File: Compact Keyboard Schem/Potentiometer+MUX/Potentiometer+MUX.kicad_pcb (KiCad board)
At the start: 2 copper layers, 83.5 x 157 mm, 17 parts, among them J1 Conn_01x04, J2 Conn_01x02, J3 Conn_01x08, J4 Conn_01x16

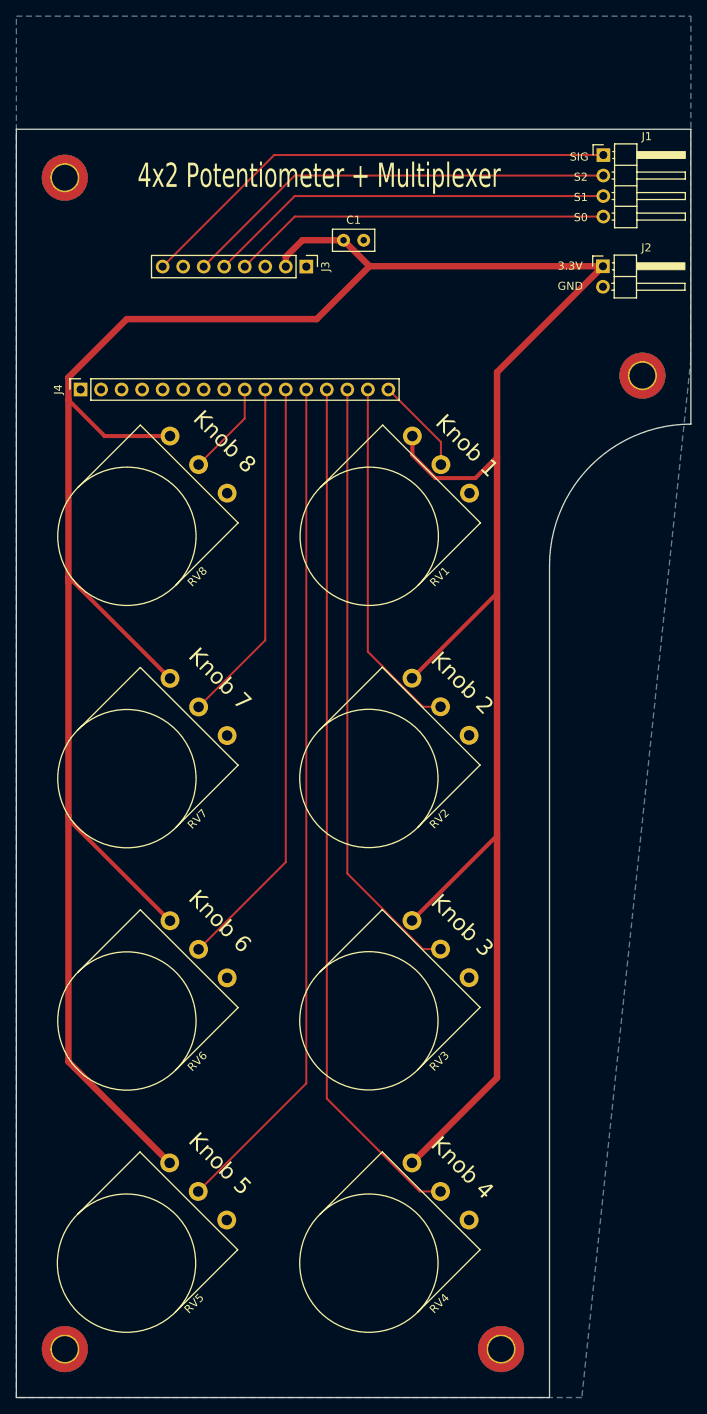
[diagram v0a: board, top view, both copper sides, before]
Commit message: Post PCB Manufacturing
Specifically the Potentiometer+ MUX
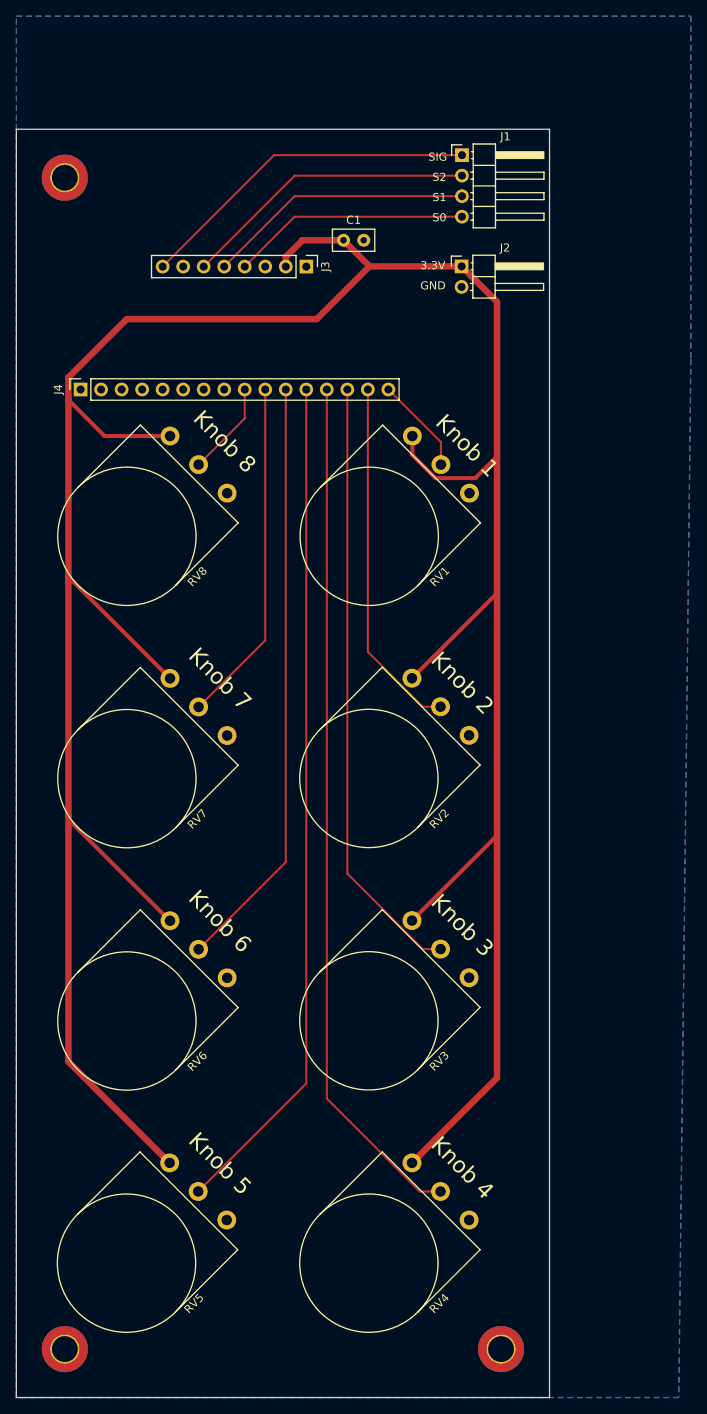
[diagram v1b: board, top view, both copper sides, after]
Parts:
- removed the REF** at (154.5, 60.5)
- moved J1 17.5 mm to (132.2, 33.2)
- moved J2 17.5 mm to (132.1, 47.0)
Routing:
- net +3.3V: track 404.8 -> 383.7 mm
- net Net-(J1-Pin_2): track 54.1 -> 36.6 mm
- net Net-(J1-Pin_4): track 47.0 -> 29.4 mm
- net Net-(J1-Pin_3): track 50.5 -> 33.0 mm
- net Net-(J1-Pin_1): track 60.3 -> 42.8 mm
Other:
- board size 83.5 x 157 mm -> 66 x 157 mm
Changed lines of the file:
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@@
 			(plot_on_all_layers_selection 0x00000000_00000000_00000000_00000000)
 			(disableapertmacros no)
-			(usegerberextensions no)
+			(usegerberextensions yes)
 			(usegerberattributes yes)
 			(usegerberadvancedattributes yes)
@@
 			(crossoutdnponfab yes)
 			(subtractmaskfromsilk no)
-			(outputformat 4)
+			(outputformat 1)
 			(mirror no)
 			(drillshape 0)
 			(scaleselection 1)
-			(outputdirectory "./")
+			(outputdirectory "Manufacturing Files/")
 		)
 	)
@@
 	(footprint "Connector_PinHeader_2.54mm:PinHeader_1x04_P2.54mm_Horizontal"
 		(layer "F.Cu")
-		(at 149.661498 33.19)
+		(at 132.161498 33.205)
 		(descr "Through hole angled pin header, 1x04, 2.54mm pitch, 6mm pin length, single row")
 		(tags "Through hole angled pin header THT 1x04 2.54mm single row")
@@
 	(footprint "MountingHole:MountingHole_3.2mm_M3_ISO7380_Pad_TopBottom"
 		(layer "F.Cu")
-		(at 154.5 60.5)
-		(descr "Mounting Hole 3.2mm, M3, generated by kicad-footprint-generator mountinghole.py")
-		(tags "mountinghole M3 ISO7380")
-		(property "Reference" "REF**"
-			(at 0 -3.8 0)
-			(layer "F.SilkS")
-			(hide yes)
-			(effects
-				(font
-					(size 1 1)
-					(thickness 0.15)
-				)
-			)
-		)
-		(property "Value" "MountingHole_3.2mm_M3_ISO7380_Pad_TopBottom"
-			(at 0 3.8 0)
-			(layer "F.Fab")
-			(effects
-				(font
-					(size 1 1)
-					(thickness 0.15)
-				)
-			)
-		)
-		(property "Datasheet" ""
-			(at 0 0 0)
-			(layer "F.Fab")
-			(hide yes)
-			(effects
-				(font
-					(size 1.27 1.27)
-					(thickness 0.15)
-				)
-			)
-		)
-		(property "Description" ""
-			(at 0 0 0)
-			(layer "F.Fab")
-			(hide yes)
-			(effects
-				(font
-					(size 1.27 1.27)
-					(thickness 0.15)
-				)
-			)
-		)
-		(attr exclude_from_pos_files exclude_from_bom)
-		(fp_circle
-			(center 0 0)
-			(end 2.85 0)
-			(stroke
-				(width 0.15)
-				(type solid)
-			)
-			(fill no)
-			(layer "Cmts.User")
-		)
-		(fp_circle
-			(center 0 0)
-			(end 3.1 0)
-			(stroke
-				(width 0.05)
-				(type solid)
-			)
-			(fill no)
-			(layer "F.CrtYd")
-		)
-		(fp_text user "${REFERENCE}"
-			(at 0 0 0)
-			(layer "F.Fab")
-			(effects
-				(font
-					(size 1 1)
-					(thickness 0.15)
-				)
-			)
-		)
-		(pad "1" thru_hole circle
-			(at 0 0)
-			(size 3.6 3.6)
-			(drill 3.2)
-			(layers "*.Cu" "*.Mask")
-			(remove_unused_layers no)
-			(zone_connect 2)
-		)
-		(pad "1" connect circle
-			(at 0 0)
-			(size 5.7 5.7)
-			(layers "F.Cu" "F.Mask")
-			(zone_connect 2)
-		)
-		(pad "1" connect circle
-			(at 0 0)
-			(size 5.7 5.7)
-			(layers "B.Cu" "B.Mask")
-			(zone_connect 2)
-		)
-		(embedded_fonts no)
-	)
-	(footprint "MountingHole:MountingHole_3.2mm_M3_ISO7380_Pad_TopBottom"
-		(layer "F.Cu")
 		(at 83 181)
 		(descr "Mounting Hole 3.2mm, M3, generated by kicad-footprint-generator mountinghole.py")
@@
 	(footprint "Connector_PinHeader_2.54mm:PinHeader_1x02_P2.54mm_Horizontal"
 		(layer "F.Cu")
-		(at 149.615 46.96)
+		(at 132.115 46.975)
 		(descr "Through hole angled pin header, 1x02, 2.54mm pitch, 6mm pin length, single row")
 		(tags "Through hole angled pin header THT 1x02 2.54mm single row")
@@
 	)
 	(gr_line
-		(start 160.5 66.5)
-		(end 160.5 30)
-		(stroke
-			(width 0.05)
-			(type default)
-		)
-		(layer "Edge.Cuts")
-	)
-	(gr_line
 		(start 143 187)
-		(end 143 84)
+		(end 143 30)
 		(stroke
 			(width 0.05)
@@
 		(layer "Edge.Cuts")
 	)
-	(gr_arc
-		(start 143 84)
-		(mid 148.125631 71.625631)
-		(end 160.5 66.5)
-		(stroke
-			(width 0.05)
-			(type default)
-		)
-		(layer "Edge.Cuts")
-	)
 	(gr_line
-		(start 160.5 30)
+		(start 143 30)
 		(end 77 30)
 		(stroke
@@
 	)
 	(gr_text "3.3V"
-		(at 144 47.5 0)
+		(at 127 47.445 0)
 		(layer "F.SilkS")
 		(effects
@@
 	)
 	(gr_text "S1"
-		(at 146 39 0)
+		(at 128.5 39.015 0)
 		(layer "F.SilkS")
 		(effects
@@
 	)
 	(gr_text "S0"
-		(at 146 41.5 0)
+		(at 128.5 41.515 0)
 		(layer "F.SilkS")
 		(effects
@@
 	)
 	(gr_text "GND"
-		(at 144 50 0)
+		(at 127 49.945 0)
 		(layer "F.SilkS")
 		(effects
@@
 		)
 	)
-	(gr_text "4x2 Potentiometer + Multiplexer"
-		(at 92 37.5 0)
-		(layer "F.SilkS")
-		(effects
-			(font
-				(size 3 2)
-				(thickness 0.25)
-			)
-			(justify left bottom)
-		)
-	)
 	(gr_text "Knob 3"
 		(at 128 126 315)
@@
 	)
 	(gr_text "SIG"
-		(at 145.5 34 0)
+		(at 128 34.015 0)
 		(layer "F.SilkS")
 		(effects
@@
 	)
 	(gr_text "S2"
-		(at 146 36.5 0)
+		(at 128.5 36.515 0)
 		(layer "F.SilkS")
 		(effects
@@
 		)
 	)
+	(gr_text "4x2 Potentiometer + Multiplexer"
+		(at 79.25 91.5 270)
+		(layer "B.SilkS")
+		(effects
+			(font
+				(size 3 2)
+				(thickness 0.25)
+			)
+			(justify left bottom mirror)
+		)
+	)
 	(gr_text_box "Designed by Aldrome"
-		(start 99.5 35.25)
-		(end 133.5 39.75)
+		(start 136.75 55.75)
+		(end 141.25 89.75)
 		(margins 1.0025 1.0025 1.0025 1.0025)
+		(angle 270)
 		(layer "B.SilkS")
 		(effects
@@
 	)
 	(segment
+		(start 120.72 46.96)
+		(end 120.735 46.975)
+		(width 0.8)
+		(layer "F.Cu")
+		(net 1)
+	)
+	(segment
 		(start 136.5 87.5)
 		(end 136.5 117.5)
@@
 	)
 	(segment
+		(start 120.735 46.975)
+		(end 132.115 46.975)
+		(width 0.8)
+		(layer "F.Cu")
+		(net 1)
+	)
+	(segment
 		(start 96.010964 127.989037)
 		(end 83.449 115.427073)
@@
 	)
 	(segment
-		(start 149.615 46.96)
-		(end 136.5 60.075)
-		(width 0.8)
-		(layer "F.Cu")
-		(net 1)
-	)
-	(segment
 		(start 120.72 46.96)
 		(end 117.5 43.74)
@@
 	)
 	(segment
+		(start 136.5 70.5)
+		(end 136.5 51.36)
+		(width 0.8)
+		(layer "F.Cu")
+		(net 1)
+	)
+	(segment
 		(start 128.865312 73.184608)
 		(end 133.815392 73.184608)
@@
 	)
 	(segment
-		(start 149.615 46.96)
-		(end 120.72 46.96)
+		(start 136.5 51.36)
+		(end 132.115 46.975)
 		(width 0.8)
 		(layer "F.Cu")
@@
 	)
 	(segment
-		(start 136.5 60.075)
-		(end 136.5 70.5)
-		(width 0.8)
-		(layer "F.Cu")
-		(net 1)
-	)
-	(segment
-		(start 149.661498 38.27)
-		(end 111.460001 38.27)
+		(start 132.161498 38.285)
+		(end 111.445001 38.285)
 		(width 0.25)
 		(layer "F.Cu")
@@
 	)
 	(segment
-		(start 111.460001 38.27)
+		(start 111.445001 38.285)
 		(end 102.730001 47)
 		(width 0.25)
@@
 	)
 	(segment
-		(start 149.661498 35.73)
-		(end 111.460001 35.73)
+		(start 111.445001 35.745)
+		(end 100.190001 47)
 		(width 0.25)
 		(layer "F.Cu")
@@
 	)
 	(segment
-		(start 111.460001 35.73)
-		(end 100.190001 47)
+		(start 132.161498 35.745)
+		(end 111.445001 35.745)
 		(width 0.25)
 		(layer "F.Cu")
@@
 	)
 	(segment
-		(start 108.92 33.19)
+		(start 108.905 33.205)
 		(end 95.11 47)
 		(width 0.25)
@@
 	)
 	(segment
-		(start 149.661498 33.19)
-		(end 108.92 33.19)
+		(start 132.161498 33.205)
+		(end 108.905 33.205)
 		(width 0.25)
 		(layer "F.Cu")
@@
 	)
 	(segment
-		(start 149.661498 40.81)
-		(end 111.460001 40.81)
+		(start 132.161498 40.825)
+		(end 111.445001 40.825)
 		(width 0.25)
 		(layer "F.Cu")
@@
 	)
 	(segment
-		(start 111.460001 40.81)
+		(start 111.445001 40.825)
 		(end 105.270001 47)
 		(width 0.25)
@@
 		(polygon
 			(pts
-				(xy 148.5 54.5) (xy 148.5 66.5) (xy 160.5 66.5) (xy 160.5 54.5)
-			)
-		)
-	)
-	(zone
-		(net 0)
-		(net_name "")
-		(layers "F.Cu" "B.Cu")
-		(name "Dead Area")
-		(hatch edge 0.5)
-		(connect_pads
-			(clearance 0)
-		)
-		(min_thickness 0.25)
-		(filled_areas_thickness no)
-		(keepout
-			(tracks not_allowed)
-			(vias not_allowed)
-			(pads allowed)
-			(copperpour not_allowed)
-			(footprints allowed)
-		)
-		(placement
-			(enabled no)
-			(sheetname "")
-		)
-		(fill
-			(thermal_gap 0.5)
-			(thermal_bridge_width 0.5)
-		)
-		(polygon
-			(pts
 				(xy 77 30) (xy 77 42) (xy 89 42) (xy 89 30)
 			)
@@
 		(polygon
 			(pts
-				(xy 77 16) (xy 160.5 16) (xy 160.5 58.454058) (xy 147 187) (xy 77 187)
+				(xy 77 16) (xy 160.5 16) (xy 160.5 58.454058) (xy 159 187) (xy 77 187)
 			)
 		)

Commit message: Pushing Update
Latest version after PCB printing
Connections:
- J3 pad 7: unconnected-(J3-Pin_7-Pad7) -> GND
